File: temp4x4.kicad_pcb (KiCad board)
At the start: 2 copper layers, 51.8 x 16.3 mm, 53 parts, among them J1 NUCLEO_CN6_1-6, J2 NUCLEO_CN5_6-1, J3 4-wire RTD, J4 4-wire RTD, J5 Bypass 2nd RTD, J6 4-wire RTD, J7 4-wire RTD, J8 Bypass 2nd RTD, U1 LP5907MFX-3.3_NOPB, U2 ADS124S08IPBS

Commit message: made board bigger to allow for better separation of analog / digital domains
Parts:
- J2: value NUCLEO_CN5_6-1 -> NUCLEO_CN5_10-1; footprint Connector_PinHeader_2.54mm:PinHeader_1x06_P2.54mm_Vertical -> Connector_PinHeader_2.54mm:PinHeader_1x10_P2.54mm_Vertical
- moved J2 10.2 mm to (160.0, 127.0)
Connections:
- J2 pad 1: SCK -> Net-(J2-Pad1)
- J2 pad 2: MISO -> Net-(J2-Pad2)
- J2 pad 3: MOSI -> Net-(J2-Pad3)
- J2 pad 4: CS -> Net-(J2-Pad4)
- J2 pad 5: DRDY -> SCK
- J2 pad 6: ENABLE -> MISO
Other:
- board size 51.8 x 16.3 mm -> 51.8 x 26.4 mm

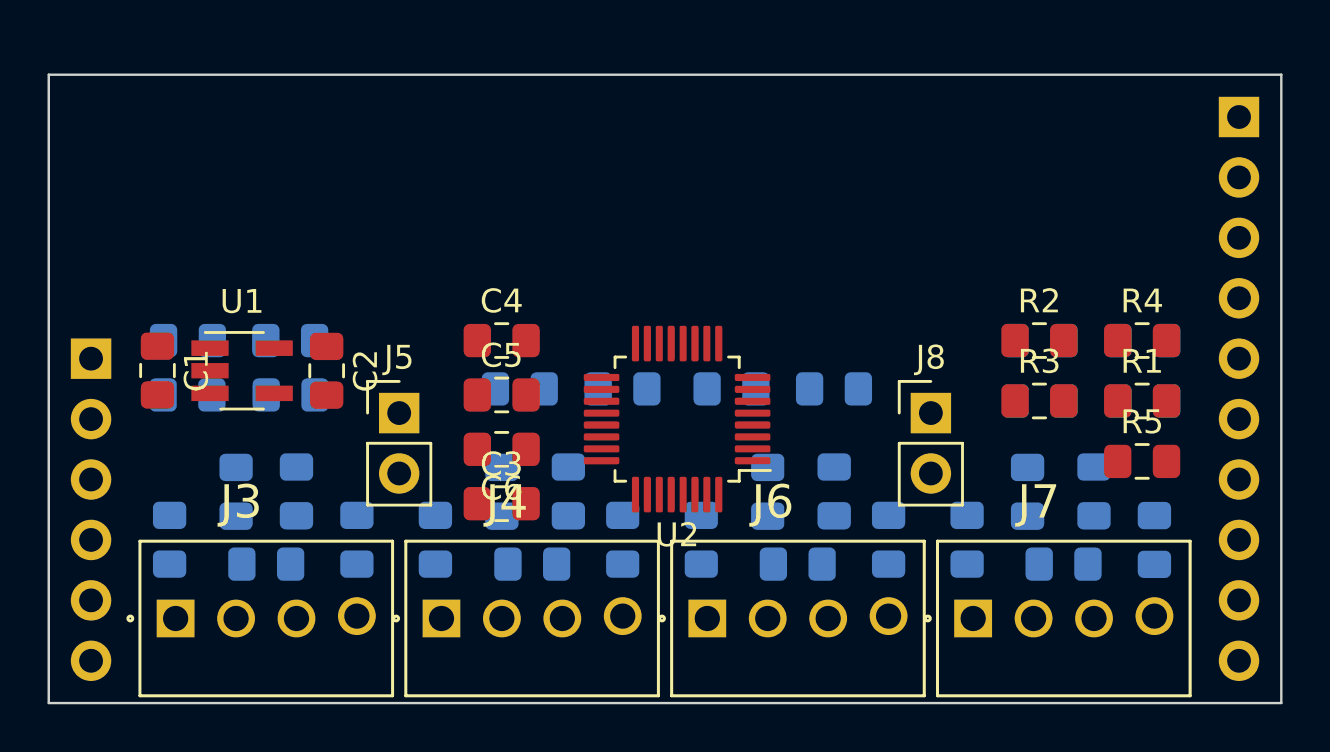
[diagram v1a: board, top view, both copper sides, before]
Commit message: re-arranged parts for better digital / analog domain separation
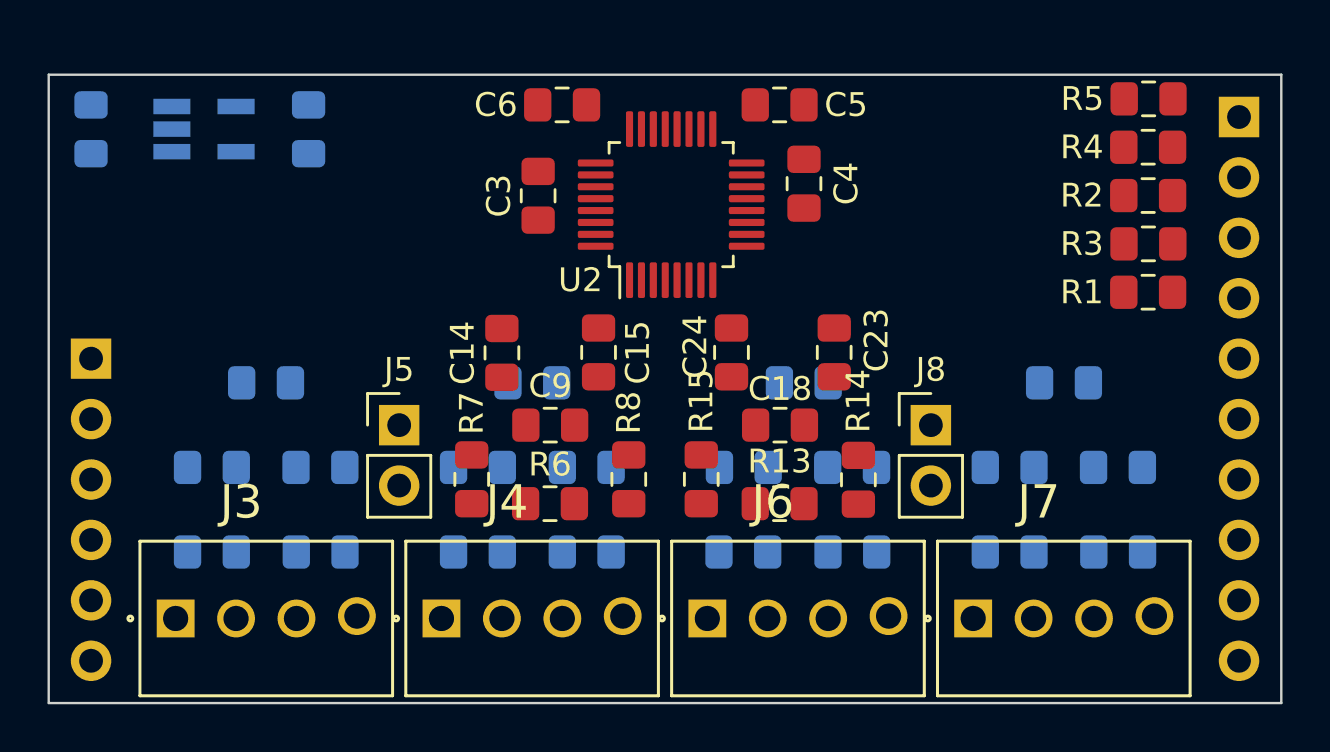
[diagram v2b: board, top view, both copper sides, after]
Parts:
- C1, C2, U1: moved to B.Cu
- C14, C15, C18, C23, C24, C9, R13, R14, R15, R6, R7, R8: moved to F.Cu
- moved R15 19.4 mm to (137.4, 142.2), turned to 90 degrees
- moved R8 19.4 mm to (134.4, 142.2), turned to 90 degrees
- moved C5 16.9 mm to (140.7, 126.5), turned to 180 degrees
- moved R13 15.8 mm to (140.7, 143.3), turned to 180 degrees
- moved C9 15.3 mm to (131.1, 140.0), turned to 0 degrees
- moved R5 15.2 mm to (156.2, 126.2)
- moved C6 14.7 mm to (131.6, 126.5)
- moved C4 14.3 mm to (141.7, 129.8), turned to 90 degrees
- moved C3 13.0 mm to (130.6, 130.3), turned to 90 degrees
- moved R6 12.9 mm to (131.1, 143.3), turned to 0 degrees
- moved C18 11.5 mm to (140.7, 140.0), turned to 180 degrees
- moved C1 10.5 mm to (111.8, 127.5), turned to 90 degrees
- moved U1 10.3 mm to (116.5, 127.5)
- moved C2 10.2 mm to (120.9, 127.5), turned to 90 degrees
- moved U2 9.02 mm to (136.1, 130.7), turned to 90 degrees
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
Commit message: changed pin connections to simplify the layout
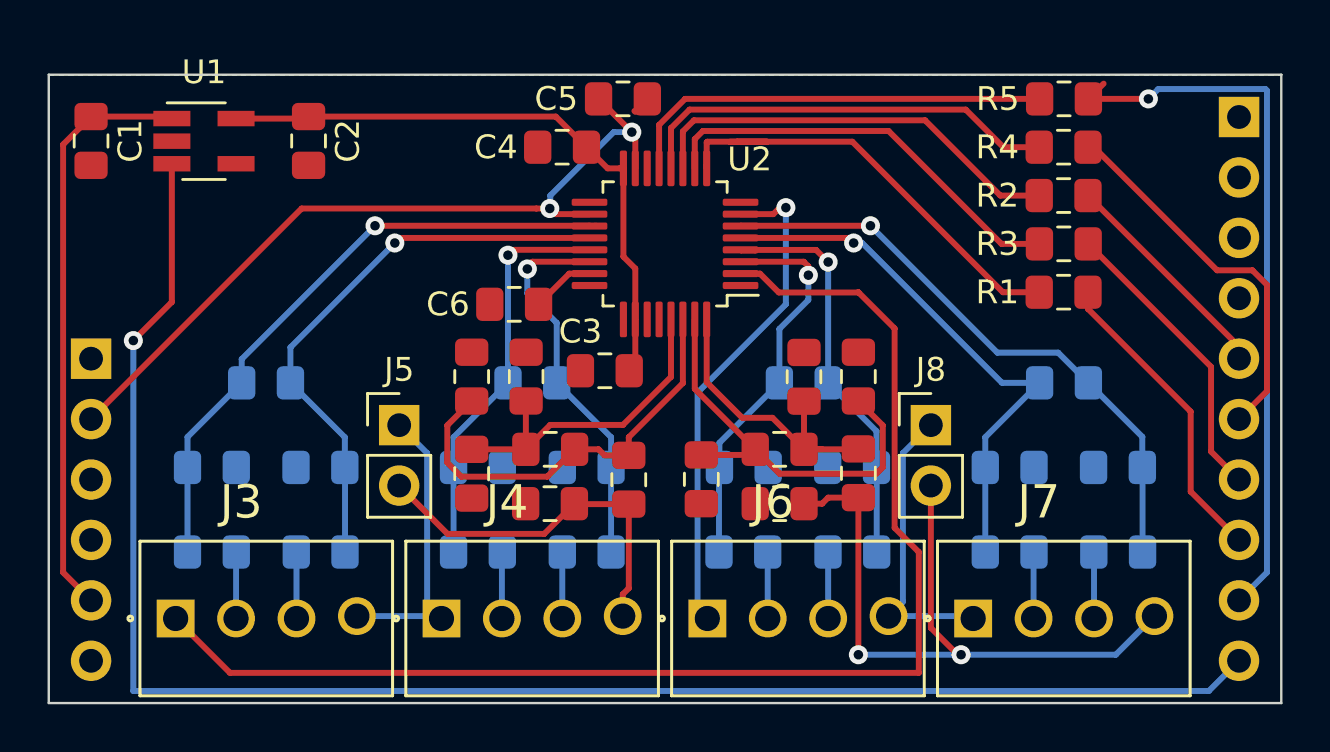
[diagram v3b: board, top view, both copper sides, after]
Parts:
- C1, C2, U1: moved to F.Cu
- moved C4 10.3 mm to (131.6, 128.3), turned to 0 degrees
- moved C6 8.62 mm to (129.5, 134.9)
- moved C3 7.87 mm to (133.4, 137.7), turned to 0 degrees
- moved R8 6.61 mm to (127.8, 142.0)
- moved R7 6.60 mm to (134.4, 142.2)
- moved C5 6.59 mm to (134.1, 126.2)
- moved C24 5.43 mm to (144.0, 137.9)
- moved R3 3.56 mm to (152.7, 132.3)
- moved R1 3.56 mm to (152.6, 134.4)
- moved R2 3.56 mm to (152.6, 130.3)
- moved R4 3.56 mm to (152.6, 128.3)
- moved R5 3.56 mm to (152.7, 126.2)
- moved C15 3.21 mm to (130.0, 137.9)
- moved U2 1.67 mm to (135.9, 132.3), turned to 180 degrees
- moved C23 1.63 mm to (141.7, 137.9)
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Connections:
- R13 pad 2: Net-(R13-Pad2) -> Earth
- R15 pad 1: Net-(R13-Pad2) -> Earth
- R6 pad 2: Net-(R6-Pad2) -> Earth
- R8 pad 1: Net-(R6-Pad2) -> Earth
- U2 pad 19: /RTD_1_2/RTD1_N -> /RTD_0_1/RTD0_P
- U2 pad 2: /RTD_1_2/IEXC -> /RTD_0_1/IEXC
- U2 pad 20: /RTD_1_2/RTD1_P -> /RTD_0_1/RTD0_N
- U2 pad 21: /RTD_1_2/RTD0_N -> /RTD_0_1/RTD1_P
- U2 pad 22: /RTD_1_2/RTD0_P -> /RTD_0_1/RTD1_N
- U2 pad 3: /RTD_0_1/RTD1_N -> /RTD_1_2/RTD0_P
- U2 pad 4: /RTD_0_1/RTD1_P -> /RTD_1_2/RTD0_N
- U2 pad 5: /RTD_0_1/RTD0_N -> /RTD_1_2/RTD1_P
- U2 pad 6: /RTD_0_1/RTD0_P -> /RTD_1_2/RTD1_N
- U2 pad 7: /RTD_0_1/IEXC -> /RTD_1_2/IEXC
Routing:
- net ENABLE: track 0.00 -> 69.8 mm, vias 0 -> 1
- net /RTD_0_1/IEXC: track 0.00 -> 54.5 mm
- net IOREF: track 0.00 -> 33.4 mm, vias 0 -> 2
- net DRDY: track 0.00 -> 30.5 mm, vias 0 -> 1
- net Net-(J7-Pad4): track 0.00 -> 29.8 mm, vias 0 -> 2
- net +3V3: track 0.00 -> 26.2 mm
- net /RTD_0_1/RTD0_P: track 0.00 -> 26.0 mm, vias 0 -> 1
- net /RTD_1_2/RTD1_N: track 0.00 -> 25.4 mm, vias 0 -> 1
- net +5V: track 0.00 -> 24.7 mm
- net /RTD_0_1/RTD0_N: track 0.00 -> 24.0 mm, vias 0 -> 1
- net /RTD_1_2/RTD1_P: track 0.00 -> 23.2 mm, vias 0 -> 1
- net /RTD_1_2/IEXC: track 0.00 -> 21.0 mm, vias 0 -> 1
- net Net-(R1-Pad1): track 0.00 -> 20.7 mm
- net Net-(R5-Pad1): track 0.00 -> 18.3 mm
- net Net-(R4-Pad1): track 0.00 -> 18.1 mm
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- added copper zone on B.Cu, net Earth
- added copper zone on F.Cu, net Earth

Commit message: added second GND connection through second pin header
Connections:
- J2 pad 4: Net-(J2-Pad4) -> Earth

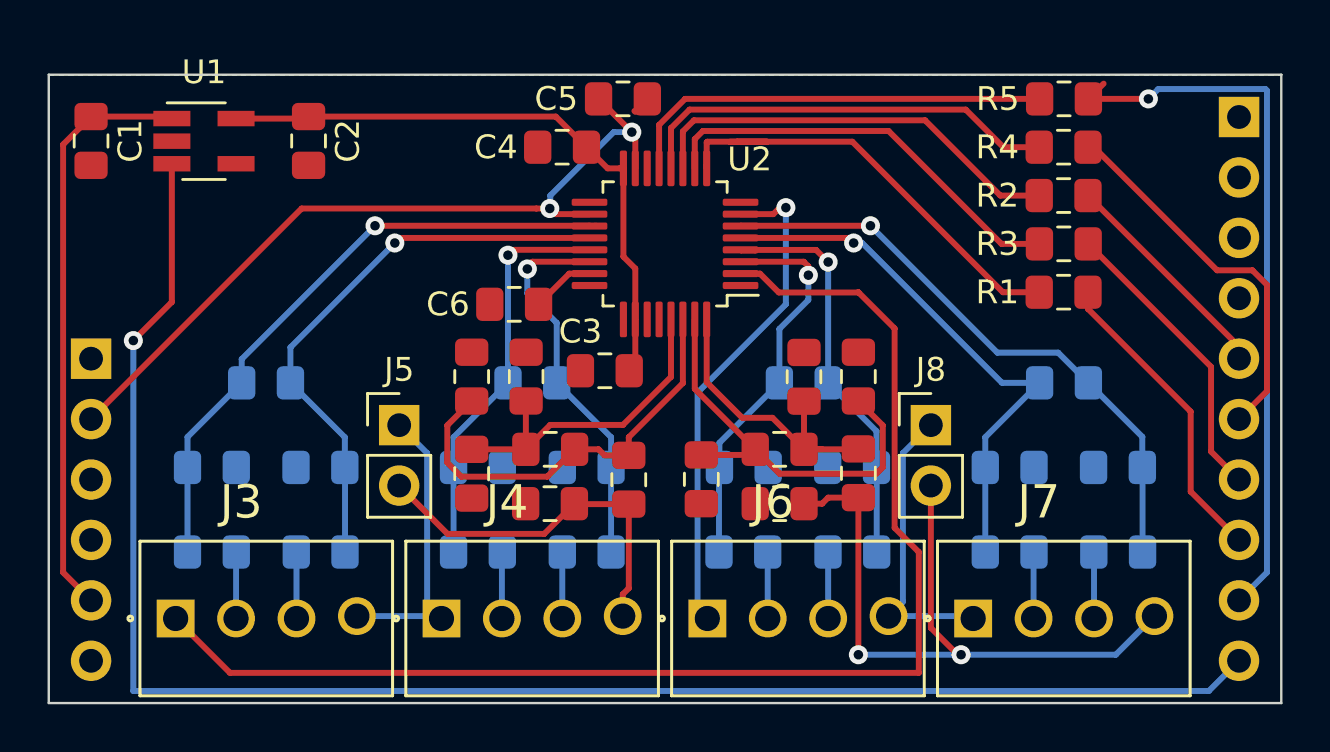
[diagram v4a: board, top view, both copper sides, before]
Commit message: shrunk the vias a bit
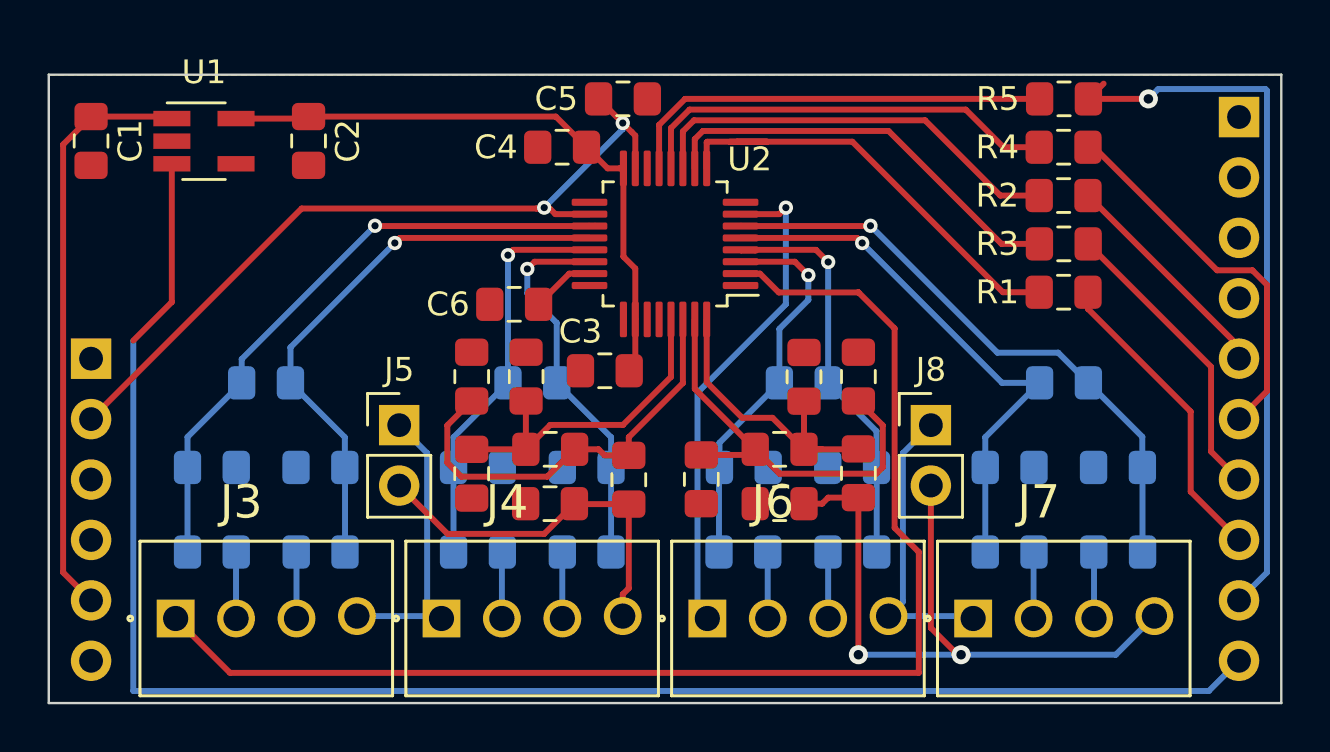
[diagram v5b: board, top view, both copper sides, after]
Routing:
- net /RTD_1_2/RTD0_N: track 16.9 -> 17.6 mm
- net ENABLE: vias 1 -> 0

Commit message: completed ground connections
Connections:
- J2 pad 4: Earth -> Net-(J2-Pad4)
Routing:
- net Earth: track 0.00 -> 200.9 mm, vias 0 -> 1
- net /RTD_0_1/IEXC: track 54.5 -> 35.7 mm, vias 0 -> 2
- net ENABLE: track 69.8 -> 73.8 mm, vias 0 -> 1
- net /RTD_1_2/IEXC: track 21.0 -> 21.6 mm
- net Net-(J7-Pad4): track 29.8 -> 29.7 mm, vias 2 -> 0
- net +3V3: vias 0 -> 2

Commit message: start re-doing the analog part
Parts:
- removed C10, C11, C12, C13, C14, C15, C19, C20, C21, C22, C23, C24: 5nF, Capacitor_SMD:C_0805_2012Metric_Pad1.15x1.40mm_HandSolder
- removed C16, C17, C18, C7, C8, C9: 50nF, Capacitor_SMD:C_0805_2012Metric_Pad1.15x1.40mm_HandSolder
- removed J3, J4, J6, J7: 4-wire RTD, temp4x4:screw_term_4x
- removed J5, J8: Bypass 2nd RTD, Connector_PinHeader_2.54mm:PinHeader_1x02_P2.54mm_Vertical
- removed R10, R11, R12, R14, R15, R16, R17, R18, R19, R7, R8, R9: 5k, Resistor_SMD:R_0805_2012Metric_Pad1.15x1.40mm_HandSolder
- removed R13, R6: 2k, Resistor_SMD:R_0805_2012Metric_Pad1.15x1.40mm_HandSolder
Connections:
- U2 pad 19: /RTD_0_1/RTD0_P -> Net-(U2-Pad19)
- U2 pad 2: /RTD_0_1/IEXC -> Net-(U2-Pad2)
- U2 pad 20: /RTD_0_1/RTD0_N -> Net-(U2-Pad20)
- U2 pad 21: /RTD_0_1/RTD1_P -> Net-(U2-Pad21)
- U2 pad 22: /RTD_0_1/RTD1_N -> Net-(U2-Pad22)
- U2 pad 29: /RTD_0_1/REF_N -> Net-(U2-Pad29)
- U2 pad 3: /RTD_1_2/RTD0_P -> Net-(U2-Pad3)
- U2 pad 30: /RTD_0_1/REF_P -> Net-(U2-Pad30)
- U2 pad 31: /RTD_1_2/REF_N -> Net-(U2-Pad31)
- U2 pad 32: /RTD_1_2/REF_P -> Net-(U2-Pad32)
- U2 pad 4: /RTD_1_2/RTD0_N -> Net-(U2-Pad4)
- U2 pad 5: /RTD_1_2/RTD1_P -> Net-(U2-Pad5)
- U2 pad 6: /RTD_1_2/RTD1_N -> Net-(U2-Pad6)
- U2 pad 7: /RTD_1_2/IEXC -> Net-(U2-Pad7)
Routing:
- net Earth: track 200.9 -> 0.00 mm, vias 1 -> 0
- net ENABLE: track 73.8 -> 0.00 mm, vias 1 -> 0
- net /RTD_0_1/IEXC: track 35.7 -> 0.00 mm, vias 2 -> 0
- net IOREF: track 33.2 -> 0.00 mm, vias 2 -> 0
- net DRDY: track 30.5 -> 0.00 mm, vias 1 -> 0
- net Net-(J7-Pad4): track 29.7 -> 0.00 mm
- net +3V3: track 26.2 -> 0.00 mm, vias 2 -> 0
- net /RTD_0_1/RTD0_P: track 26.0 -> 0.00 mm, vias 1 -> 0
- net /RTD_1_2/RTD1_N: track 25.4 -> 0.00 mm, vias 1 -> 0
- net +5V: track 24.7 -> 0.00 mm
- net /RTD_0_1/RTD0_N: track 24.0 -> 0.00 mm, vias 1 -> 0
- net /RTD_1_2/RTD1_P: track 23.2 -> 0.00 mm, vias 1 -> 0
- net /RTD_1_2/IEXC: track 21.6 -> 0.00 mm, vias 1 -> 0
- net Net-(R1-Pad1): track 20.7 -> 0.00 mm
- net Net-(R5-Pad1): track 18.3 -> 0.00 mm
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
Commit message: re-done analog part of the circuit
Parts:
- added C10: C, Capacitor_SMD:C_0805_2012Metric_Pad1.15x1.40mm_HandSolder, B.Cu at (141.5, 138.9)
- added C11: C, Capacitor_SMD:C_0805_2012Metric_Pad1.15x1.40mm_HandSolder, B.Cu at (139.2, 142.2)
- added C12: C, Capacitor_SMD:C_0805_2012Metric_Pad1.15x1.40mm_HandSolder, B.Cu at (121.4, 142.2)
- added C13: C, Capacitor_SMD:C_0805_2012Metric_Pad1.15x1.40mm_HandSolder, B.Cu at (119.1, 138.9)
- added C14: C, Capacitor_SMD:C_0805_2012Metric_Pad1.15x1.40mm_HandSolder, B.Cu at (116.8, 142.2)
- added C16: C, Capacitor_SMD:C_0805_2012Metric_Pad1.15x1.40mm_HandSolder, B.Cu at (132.6, 142.2)
- added C17: C, Capacitor_SMD:C_0805_2012Metric_Pad1.15x1.40mm_HandSolder, B.Cu at (130.3, 138.9)
- added C18: C, Capacitor_SMD:C_0805_2012Metric_Pad1.15x1.40mm_HandSolder, B.Cu at (128.0, 142.2)
- added C19: C, Capacitor_SMD:C_0805_2012Metric_Pad1.15x1.40mm_HandSolder, F.Cu at (147.8, 139.2)
- added C20: C, Capacitor_SMD:C_0805_2012Metric_Pad1.15x1.40mm_HandSolder, F.Cu at (143.2, 142.5)
- added C21: C, Capacitor_SMD:C_0805_2012Metric_Pad1.15x1.40mm_HandSolder, F.Cu at (143.3, 139.2)
- added C5: C, Capacitor_SMD:C_0805_2012Metric_Pad1.15x1.40mm_HandSolder, B.Cu at (154.9, 142.2)
- added C7: C, Capacitor_SMD:C_0805_2012Metric_Pad1.15x1.40mm_HandSolder, B.Cu at (152.6, 138.9)
- added C8: C, Capacitor_SMD:C_0805_2012Metric_Pad1.15x1.40mm_HandSolder, B.Cu at (150.4, 142.2)
- added C9: C, Capacitor_SMD:C_0805_2012Metric_Pad1.15x1.40mm_HandSolder, B.Cu at (143.8, 142.2)
- added J1: RTD1, temp4x4:screw_term_4x, F.Cu at (148.8, 148.1)
- added J3: RTD1, temp4x4:screw_term_4x, F.Cu at (137.7, 148.1)
- added J5: RTD1, temp4x4:screw_term_4x, F.Cu at (115.3, 148.1)
- added J6: RTD1, temp4x4:screw_term_4x, F.Cu at (126.5, 148.1)
- added R10: R, Resistor_SMD:R_0805_2012Metric_Pad1.15x1.40mm_HandSolder, B.Cu at (121.4, 145.5)
- added R11: R, Resistor_SMD:R_0805_2012Metric_Pad1.15x1.40mm_HandSolder, B.Cu at (116.8, 145.5)
- added R12: R, Resistor_SMD:R_0805_2012Metric_Pad1.15x1.40mm_HandSolder, B.Cu at (132.6, 145.5)
- added R13: R, Resistor_SMD:R_0805_2012Metric_Pad1.15x1.40mm_HandSolder, B.Cu at (128.0, 145.5)
- added R14: R, Resistor_SMD:R_0805_2012Metric_Pad1.15x1.40mm_HandSolder, F.Cu at (151.1, 141.0)
- added R15: R, Resistor_SMD:R_0805_2012Metric_Pad1.15x1.40mm_HandSolder, F.Cu at (147.8, 142.5)
- added R16: R, Resistor_SMD:R_0805_2012Metric_Pad1.15x1.40mm_HandSolder, F.Cu at (140.0, 141.0)
- added R3: R, Resistor_SMD:R_0805_2012Metric_Pad1.15x1.40mm_HandSolder, B.Cu at (154.9, 145.5)
- added R6: R, Resistor_SMD:R_0805_2012Metric_Pad1.15x1.40mm_HandSolder, B.Cu at (150.4, 145.5)
- added R8: R, Resistor_SMD:R_0805_2012Metric_Pad1.15x1.40mm_HandSolder, B.Cu at (143.8, 145.5)
- added R9: R, Resistor_SMD:R_0805_2012Metric_Pad1.15x1.40mm_HandSolder, B.Cu at (139.2, 145.5)
- renumbered C6 to C15, C5 to C6, J1 to J2, J2 to J4, R3 to R4, R4 to R5, R5 to R7
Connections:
- C2 pad 2: Earth -> Net-(C2-Pad2)
- U1 pad 2: Earth -> Net-(C2-Pad2)
